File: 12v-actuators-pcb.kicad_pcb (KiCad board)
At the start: 2 copper layers, 83 x 80 mm, 211 parts, among them J1 690367280876, J10 ESC_35_1_P, J11 690367280876, J12 ESC_35_2_S, J13 Alim Pompe, J14 690367280876, J16 690367280876, J17 690367280876, J18 690367280876, J19 Alim EV, J2 3.5mm WR-TBL, J20 Alim EV, J21 Alim EV, J22 Alim EV, J23 Alim EV, J24 Alim EV, J25 Alim EV, J26 Alim EV, J27 Alim EV, J28 Alim EV, J29 Alim EV, J3 690367280676, J30 Alim EV, J4 STLINK, J5 65100516121, J6 ESC_35_1_P, J7 RGBA_LEDs, J8 CAN, J9 ESC_35_1_S, Q1 G2302, Q10 G2302, Q11 G2302, Q12 G2302, Q13 G2302, Q14 G2302, Q15 G2302, Q16 G2302, Q17 G2302, Q18 G2302, Q2 G2302, Q3 G2302, Q4 G2302, Q5 G2302, Q6 SUM110P06-08L, Q7 2N7002, Q8 2N7002, SW1 435431019840, U1 MCP2551-I-SN, U2 TCA9517DR, U3 WSEN-PDUS, U4 STM32G474CEUx, U5 AMS1117-3.3, U6 TPS82130, Y1 16 MHz

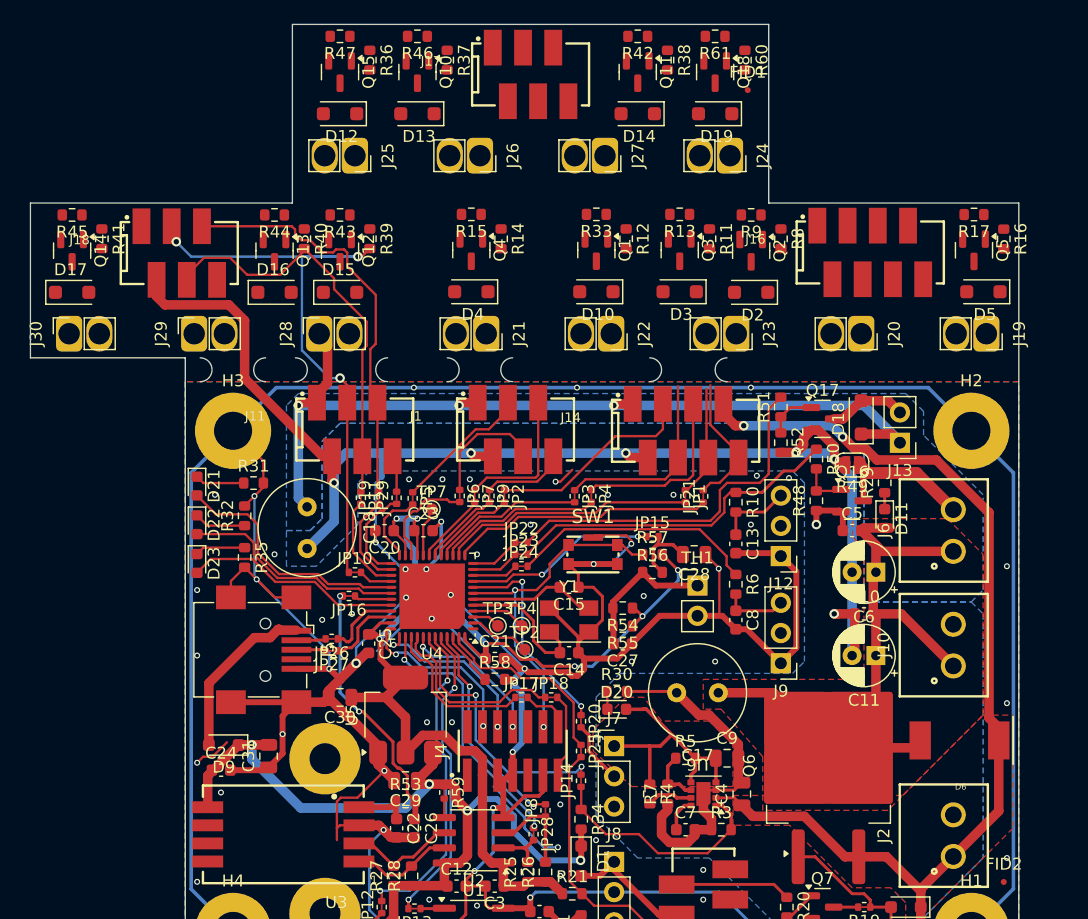
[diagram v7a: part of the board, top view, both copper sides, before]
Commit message: debut routage carte peripherique
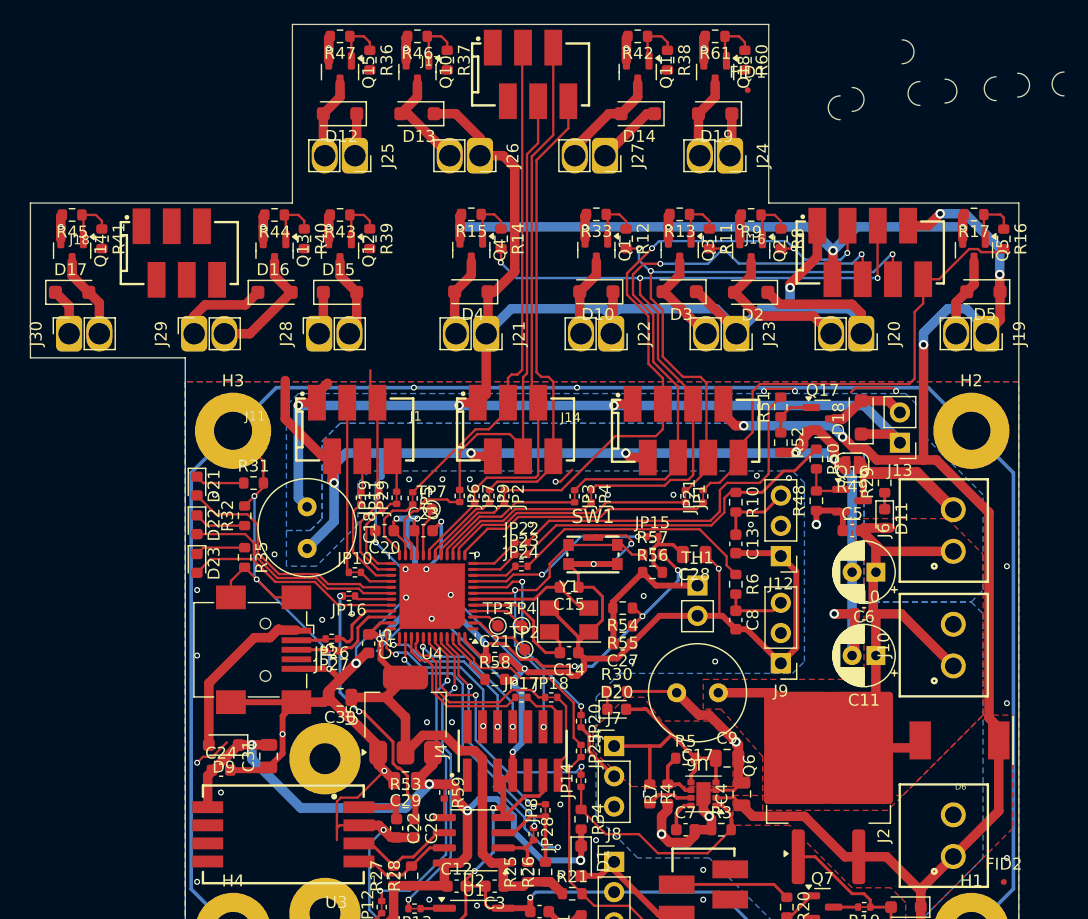
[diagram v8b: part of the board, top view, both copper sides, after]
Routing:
- net /PWR_12V: track 133.1 -> 253.2 mm, vias 3 -> 4
- net GNDPWR: track 151.0 -> 206.6 mm, vias 8 -> 24
- net /EV_3: track 15.1 -> 65.2 mm, vias 0 -> 3
- net /EV_4: track 9.45 -> 48.8 mm, vias 0 -> 3
- net /EV_9: track 51.9 -> 14.3 mm, vias 3 -> 0
- net /EV_1: track 17.5 -> 53.7 mm, vias 0 -> 3
- net /EV_2: track 16.2 -> 51.5 mm, vias 0 -> 3
- net /VBATT_12V: track 88.2 -> 123.0 mm, vias 2 -> 5
- net /EV_10: track 35.3 -> 3.03 mm
- net /EV_8: track 7.01 -> 38.9 mm
- net /EV_7: track 11.9 -> 42.7 mm
- net /EV_5: track 11.5 -> 42.1 mm
- net /EV_6: track 10.4 -> 40.7 mm
- net /EV_P: track 11.5 -> 41.6 mm
- net /EV_11: track 35.1 -> 10.5 mm
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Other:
- board size 83 x 80 mm -> 86.8 x 80 mm
